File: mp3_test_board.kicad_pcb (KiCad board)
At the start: 2 copper layers, 12 parts, among them U1 RT6222D, U10 OPA1652, U11 LM4562, U12 W25Q128JVSIQ, U13 F1C200S, U2 RT9829, U3 RT4812, U4 RT9525, U5 SN74LVC2G74, U6 RT5750A, U7 RT5750A, U9 WM8741

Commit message: added crystal,backlight regulator and usb nets
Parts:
- removed U1: RT6222D, Package_TO_SOT_SMD:TSOT-23-6
- removed U10: OPA1652, rlib_ic:SOIC-8_3.9x4.9mm_P1.27mm
- removed U11: LM4562, rlib_ic:SOIC-8_3.9x4.9mm_P1.27mm
- removed U12: W25Q128JVSIQ, rlib_ic:SOIC-8_5.23x5.23mm_P1.27mm
- removed U13: F1C200S, rlib_ic:QFN-88_EP_10x10_Pitch0.4mm
- removed U2: RT9829, Package_DFN_QFN:DFN-8_2x2mm_P0.5mm
- removed U3: RT4812, Package_TO_SOT_SMD:TSOT-23-8
- removed U4: RT9525, Package_DFN_QFN:QFN-16-1EP_3x3mm_P0.5mm_EP1.45x1.45mm
- removed U5: SN74LVC2G74, Package_SO:SSOP-8_3.9x5.05mm_P1.27mm
- removed U6, U7: RT5750A, Package_TO_SOT_SMD:SOT-23-5
- removed U9: WM8741, rlib_ic:SSOP-28_5.3x10.2mm_P0.65mm
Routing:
- net Net-(C41-Pad1): track 23.6 -> 0.00 mm
- net +5VA: track 18.8 -> 0.00 mm

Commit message: changed volume buttons
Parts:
- added J2: PJ-3270, rlib_connectors:PJ-3270, F.Cu at (191.1, 128.3)
- added J3: TF01-A, rlib_connectors:TF-01A, F.Cu at (150.3, 130.8)
- added P1: HRO-TYPE-C-31-M-12, rlib_connectors:HRO-TYPE-C-31-M-12, F.Cu at (191.2, 112.5)
- added SW1: TS-1010-C-A, rlib_buttons:TS-1010-X-X, F.Cu at (110.6, 134.0)
- added SW7: TS-1010-C-A, rlib_buttons:TS-1010-X-X, F.Cu at (132.9, 133.9)
- added SW8: TS-1010-C-A, rlib_buttons:TS-1010-X-X, F.Cu at (122.6, 134.0)
- added U1: RT5750A, rlib_power:SOT-23-5, F.Cu at (174.6, 101.0)
- added U10: OPA1652, rlib_ic:SOIC-8_3.9x4.9mm_P1.27mm, F.Cu at (148.0, 92.1)
- added U11: LM4562, rlib_ic:SOIC-8_3.9x4.9mm_P1.27mm, F.Cu at (148.6, 101.6)
- added U12: W25Q128JVSIQ, rlib_ic:SOIC-8_5.23x5.23mm_P1.27mm, F.Cu at (131.4, 116.2)
- added U2: RT9467, rlib_power:WQFN-24-1EP_4x4mm_P0.5mm_EP2.45x2.45mm, F.Cu at (161.3, 120.7)
- added U3: RT4812, rlib_power:TSOT-23-8, F.Cu at (175.3, 116.2)
- added U4: F1C200S, rlib_ic:QFN-88_EP_10x10_Pitch0.4mm, F.Cu at (117.4, 116.1)
- added U5: RT6150, rlib_power:RT6150AGQW, F.Cu at (168.9, 108.6)
- added U6: RT5750A, rlib_power:SOT-23-5, F.Cu at (165.7, 101.0)
- added U7: RT5750A, rlib_power:SOT-23-5, F.Cu at (174.6, 108.0)
- added U8: USBLC6-2SC6, Package_TO_SOT_SMD:SOT-23-6, F.Cu at (136.5, 99.2)
- added U9: WM8741, rlib_ic:SSOP-28_5.3x10.2mm_P0.65mm, F.Cu at (123.2, 102.2)
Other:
- board outline added: 131.4 x 66.7 mm

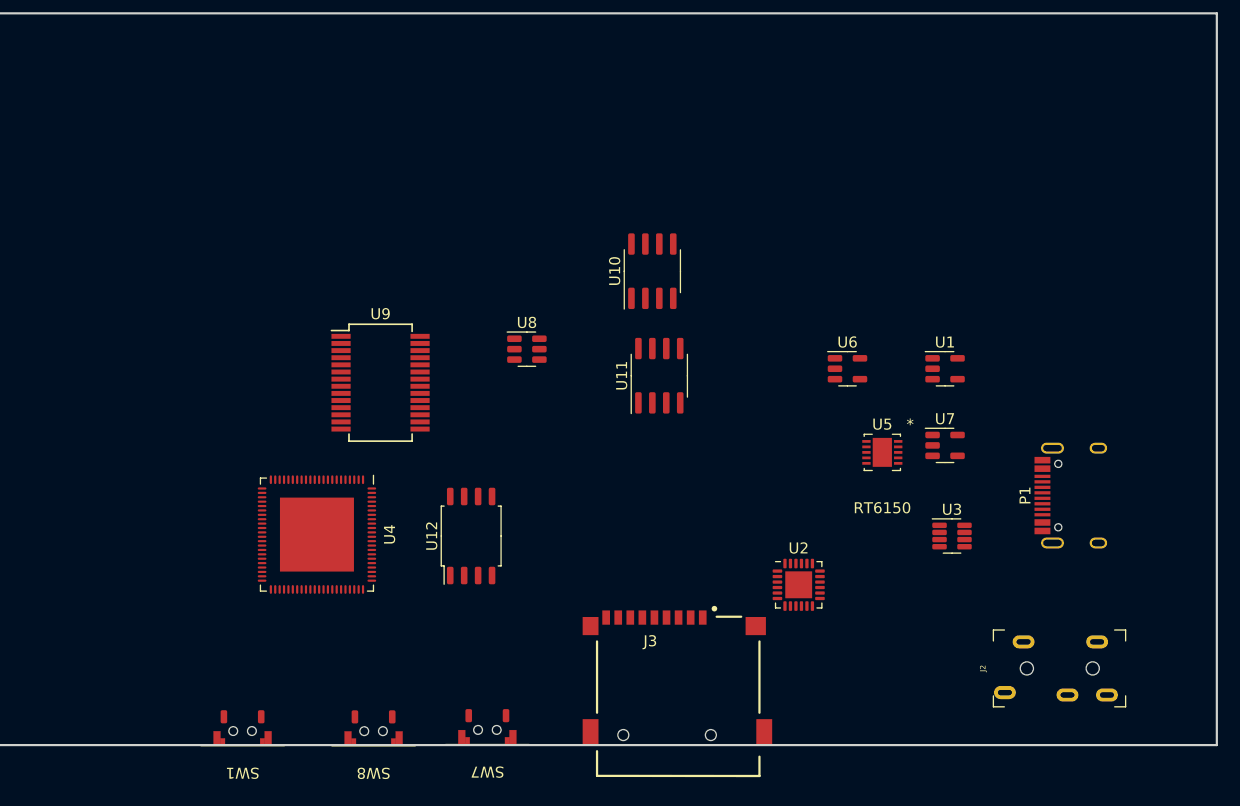
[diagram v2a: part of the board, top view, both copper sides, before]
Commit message: added buttons
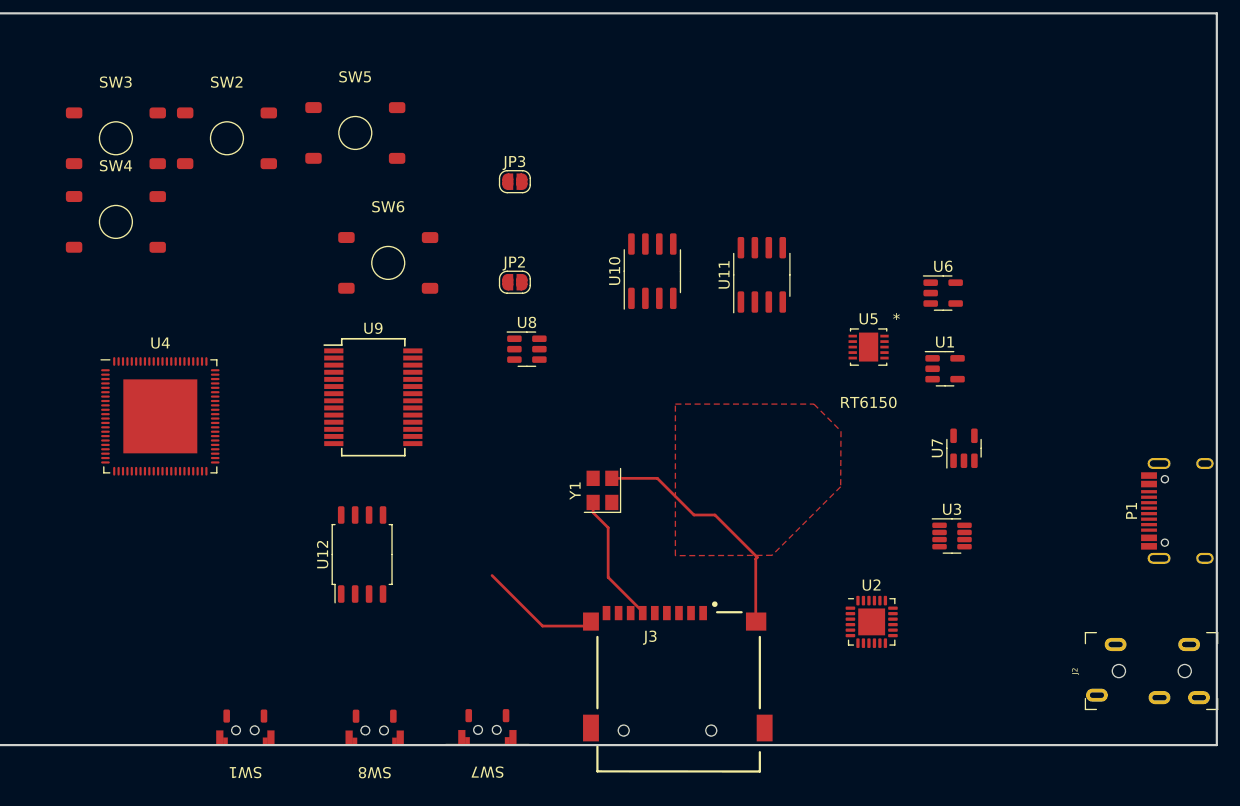
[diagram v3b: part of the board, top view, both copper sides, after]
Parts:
- added JP2: Reset, Jumper:SolderJumper-2_P1.3mm_Open_RoundedPad1.0x1.5mm, F.Cu at (135.4, 93.1)
- added JP3: Jumper_2_Open, Jumper:SolderJumper-2_P1.3mm_Open_RoundedPad1.0x1.5mm, F.Cu at (135.4, 83.9)
- added SW2: TS-1157-X-A, rlib_buttons:TS-1157-X-A, F.Cu at (109.2, 80.0)
- added SW3: TS-1157-X-A, rlib_buttons:TS-1157-X-A, F.Cu at (99.1, 80.0)
- added SW4: TS-1157-X-A, rlib_buttons:TS-1157-X-A, F.Cu at (99.1, 87.6)
- added SW5: TS-1157-X-A, rlib_buttons:TS-1157-X-A, F.Cu at (120.9, 79.5)
- added SW6: TS-1157-X-A, rlib_buttons:TS-1157-X-A, F.Cu at (123.9, 91.3)
- added Y1: Crystal_GND24, rlib_crystals:Crystal_SMD_Abracon_ABM8G-4Pin_3.2x2.5mm, F.Cu at (143.4, 112.0)
- moved U4 17.9 mm to (103.1, 105.3), turned to 0 degrees
- moved U11 13.1 mm to (157.9, 92.4)
- moved U6 11.1 mm to (174.5, 94.1)
- moved U12 10.1 mm to (121.5, 117.9)
- moved P1 9.81 mm to (200.9, 113.9)
- moved U5 9.68 mm to (167.7, 99.0)
- moved J2 8.39 mm to (199.5, 128.5)
- moved U2 7.46 mm to (167.9, 124.0)
- moved U7 1.74 mm to (176.3, 108.2), turned to 90 degrees
- moved U9 1.48 mm to (122.5, 103.6)
- moved J3 0.41 mm to (150.3, 130.4)
- moved SW1 0.26 mm to (110.9, 133.9)
- moved SW8 0.12 mm to (122.7, 133.9)
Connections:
- U4 pad 60: AUDIO_PLUG -> Net-(U4-Pad60)
- U4 pad 62: unconnected-(U4-Pad62) -> AUDIO_PLUG
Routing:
- net GND: track 0.00 -> 45.8 mm
- added copper zone on F.Cu, net /SOC/LCD_D10

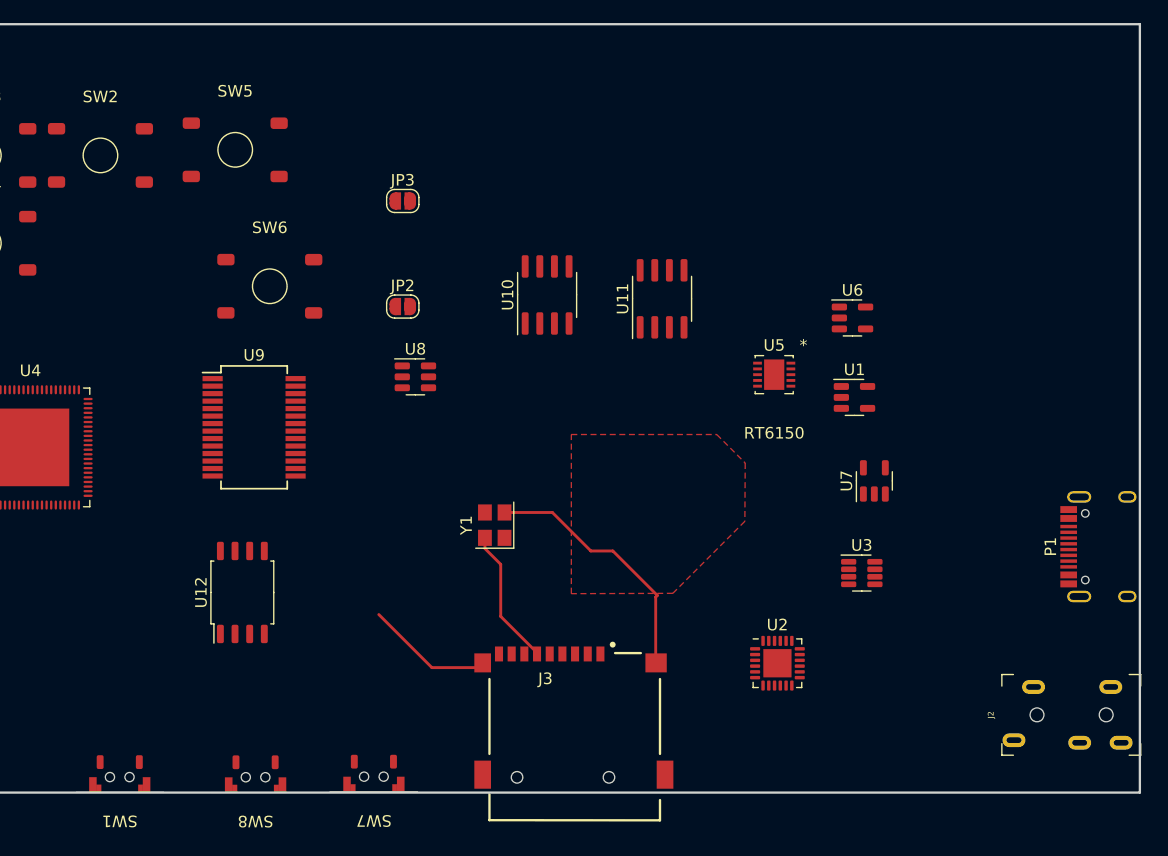
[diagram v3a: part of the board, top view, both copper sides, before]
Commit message: adde power source 3v0, molex connector, restistor footprints
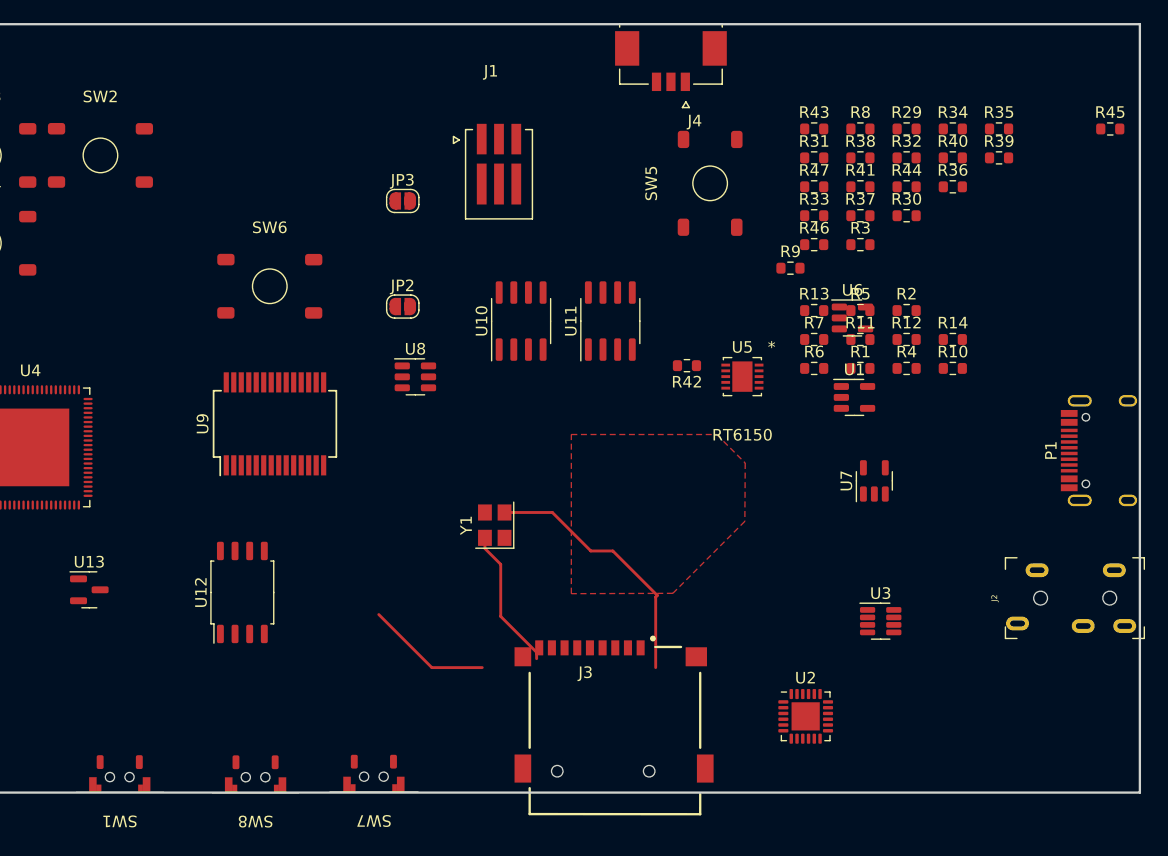
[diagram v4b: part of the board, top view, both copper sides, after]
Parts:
- added J1: 874380343, rlib_connectors:MOLEX_874380343, F.Cu at (143.8, 81.6)
- added J4: 532610371, rlib_connectors:MOLEX_532610371, F.Cu at (158.7, 71.2)
- added R1: R, rlib_passive:R_0603_1608Metric, F.Cu at (175.1, 98.5)
- added R10: R, rlib_passive:R_0603_1608Metric, F.Cu at (183.2, 98.5)
- added R11: R, rlib_passive:R_0603_1608Metric, F.Cu at (175.1, 95.9)
- added R12: R, rlib_passive:R_0603_1608Metric, F.Cu at (179.2, 95.9)
- added R13: R, rlib_passive:R_0603_1608Metric, F.Cu at (171.1, 93.4)
- added R14: R, rlib_passive:R_0603_1608Metric, F.Cu at (183.2, 95.9)
- added R2: R, rlib_passive:R_0603_1608Metric, F.Cu at (179.2, 93.4)
- added R29: R, rlib_passive:R_0603_1608Metric, F.Cu at (179.2, 77.7)
- added R3: R, rlib_passive:R_0603_1608Metric, F.Cu at (175.1, 87.7)
- added R30: R, rlib_passive:R_0603_1608Metric, F.Cu at (179.2, 85.2)
- added R31: R, rlib_passive:R_0603_1608Metric, F.Cu at (171.1, 80.2)
- added R32: R, rlib_passive:R_0603_1608Metric, F.Cu at (179.2, 80.2)
- added R33: R, rlib_passive:R_0603_1608Metric, F.Cu at (171.1, 85.2)
- added R34: R, rlib_passive:R_0603_1608Metric, F.Cu at (183.2, 77.7)
- added R35: R, rlib_passive:R_0603_1608Metric, F.Cu at (187.2, 77.7)
- added R36: R, rlib_passive:R_0603_1608Metric, F.Cu at (183.2, 82.7)
- added R37: R, rlib_passive:R_0603_1608Metric, F.Cu at (175.1, 85.2)
- added R38: R, rlib_passive:R_0603_1608Metric, F.Cu at (175.1, 80.2)
- added R39: R, rlib_passive:R_0603_1608Metric, F.Cu at (187.2, 80.2)
- added R4: R, rlib_passive:R_0603_1608Metric, F.Cu at (179.2, 98.5)
- added R40: R, rlib_passive:R_0603_1608Metric, F.Cu at (183.2, 80.2)
- added R41: R, rlib_passive:R_0603_1608Metric, F.Cu at (175.1, 82.7)
- added R42: R, rlib_passive:R_0603_1608Metric, F.Cu at (160.1, 98.2)
- added R43: R, rlib_passive:R_0603_1608Metric, F.Cu at (171.1, 77.7)
- added R44: R, rlib_passive:R_0603_1608Metric, F.Cu at (179.2, 82.7)
- added R45: R, rlib_passive:R_0603_1608Metric, F.Cu at (196.8, 77.7)
- added R46: R, rlib_passive:R_0603_1608Metric, F.Cu at (171.1, 87.7)
- added R47: R, rlib_passive:R_0603_1608Metric, F.Cu at (171.1, 82.7)
- added R5: R, rlib_passive:R_0603_1608Metric, F.Cu at (175.1, 93.4)
- added R6: R, rlib_passive:R_0603_1608Metric, F.Cu at (171.1, 98.5)
- added R7: R, rlib_passive:R_0603_1608Metric, F.Cu at (171.1, 95.9)
- added R8: R, rlib_passive:R_0603_1608Metric, F.Cu at (175.1, 77.7)
- added R9: R, rlib_passive:R_0603_1608Metric, F.Cu at (169.1, 89.8)
- added U13: XC6206P302MR, rlib_power:SOT-23, F.Cu at (108.2, 117.7)
- moved SW5 41.3 mm to (162.1, 82.4), turned to 90 degrees
- moved J2 10.1 mm to (199.8, 118.4)
- moved P1 8.34 mm to (201.0, 105.6)
- moved U2 5.22 mm to (170.4, 128.6)
- moved U11 4.89 mm to (153.4, 94.3)
- moved U3 4.49 mm to (176.9, 120.4)
- moved J3 3.53 mm to (153.8, 129.9)
- moved U10 3.20 mm to (145.7, 94.3)
- moved U5 2.77 mm to (164.9, 99.2)
- moved U9 1.83 mm to (124.3, 103.3), turned to 90 degrees

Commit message: added winstar display
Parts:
- added C1: C, rlib_passive:C_0603_1608Metric, F.Cu at (209.5, 121.0)
- added C10: C, rlib_passive:C_0603_1608Metric, F.Cu at (209.5, 123.5)
- added C11: C, rlib_passive:C_0603_1608Metric, F.Cu at (193.4, 118.5)
- added C12: C, rlib_passive:C_0603_1608Metric, F.Cu at (197.4, 121.0)
- added C13: C, rlib_passive:C_0603_1608Metric, F.Cu at (201.4, 118.5)
- added C14: C, rlib_passive:C_0603_1608Metric, F.Cu at (201.4, 126.0)
- added C15: 100n, rlib_passive:C_0603_1608Metric, F.Cu at (221.4, 93.5)
- added C16: C, rlib_passive:C_0603_1608Metric, F.Cu at (209.5, 118.5)
- added C17: C, rlib_passive:C_0603_1608Metric, F.Cu at (205.4, 118.5)
- added C18: C, rlib_passive:C_0603_1608Metric, F.Cu at (213.5, 118.5)
- added C19: C, rlib_passive:C_0603_1608Metric, F.Cu at (197.4, 126.0)
- added C2: C, rlib_passive:C_0603_1608Metric, F.Cu at (205.4, 126.0)
- added C20: C, rlib_passive:C_0603_1608Metric, F.Cu at (205.4, 121.0)
- added C21: C, rlib_passive:C_0603_1608Metric, F.Cu at (205.4, 123.5)
- added C22: C, rlib_passive:C_0603_1608Metric, F.Cu at (205.4, 116.0)
- added C26: 0.1u, rlib_passive:C_0603_1608Metric, F.Cu at (226.5, 100.0)
- added C28: 0.1u, rlib_passive:C_0603_1608Metric, F.Cu at (234.5, 97.5)
- added C3: C, rlib_passive:C_0603_1608Metric, F.Cu at (197.4, 116.0)
- added C30: 0.1u, rlib_passive:C_0603_1608Metric, F.Cu at (226.5, 97.5)
- added C32: 0.1u, rlib_passive:C_0603_1608Metric, F.Cu at (234.5, 100.0)
- added C33: 3.3n, rlib_passive:C_0603_1608Metric, F.Cu at (234.5, 95.0)
- added C34: 3.3n, rlib_passive:C_0603_1608Metric, F.Cu at (226.5, 95.0)
- added C37: 0.1u, rlib_passive:C_0603_1608Metric, F.Cu at (230.5, 95.0)
- added C38: 0.1u, rlib_passive:C_0603_1608Metric, F.Cu at (230.5, 100.0)
- added C4: C, rlib_passive:C_0603_1608Metric, F.Cu at (201.4, 123.5)
- added C45: 0.1u, rlib_passive:C_0603_1608Metric, F.Cu at (230.5, 97.5)
- added C46: 0.1u, rlib_passive:C_0603_1608Metric, F.Cu at (152.0, 171.7)
- added C47: 100n, rlib_passive:C_0603_1608Metric, F.Cu at (213.4, 96.0)
- added C48: 100n, rlib_passive:C_0603_1608Metric, F.Cu at (134.4, 175.9)
- added C49: 100n, rlib_passive:C_0603_1608Metric, F.Cu at (205.4, 101.1)
- added C5: C, rlib_passive:C_0603_1608Metric, F.Cu at (193.4, 126.0)
- added C50: 100n, rlib_passive:C_0603_1608Metric, F.Cu at (205.4, 98.5)
- added C51: C, rlib_passive:C_0603_1608Metric, F.Cu at (197.4, 123.5)
- added C52: C, rlib_passive:C_0603_1608Metric, F.Cu at (193.4, 116.0)
- added C53: C, rlib_passive:C_0603_1608Metric, F.Cu at (197.4, 118.5)
- added C54: 100n, rlib_passive:C_0603_1608Metric, F.Cu at (213.4, 93.5)
- added C55: 100n, rlib_passive:C_0603_1608Metric, F.Cu at (142.4, 175.9)
- added C56: 100n, rlib_passive:C_0603_1608Metric, F.Cu at (205.4, 93.5)
- added C57: 100n, rlib_passive:C_0603_1608Metric, F.Cu at (138.4, 175.9)
- added C58: 100n, rlib_passive:C_0603_1608Metric, F.Cu at (209.4, 96.0)
- added C59: 100n, rlib_passive:C_0603_1608Metric, F.Cu at (207.3, 106.1)
- added C6: C, rlib_passive:C_0603_1608Metric, F.Cu at (193.4, 123.5)
- added C60: 100n, rlib_passive:C_0603_1608Metric, F.Cu at (213.4, 98.5)
- added C61: 100n, rlib_passive:C_0603_1608Metric, F.Cu at (195.3, 106.3)
- added C62: 100n, rlib_passive:C_0603_1608Metric, F.Cu at (209.4, 98.5)
- added C63: 100n, rlib_passive:C_0603_1608Metric, F.Cu at (209.4, 101.1)
- added C64: 100n, rlib_passive:C_0603_1608Metric, F.Cu at (130.4, 175.9)
- added C65: 100n, rlib_passive:C_0603_1608Metric, F.Cu at (209.4, 103.6)
- added C66: 100n, rlib_passive:C_0603_1608Metric, F.Cu at (203.3, 106.3)
- added C67: 100n, rlib_passive:C_0603_1608Metric, F.Cu at (199.3, 106.3)
- added C68: 100n, rlib_passive:C_0603_1608Metric, F.Cu at (205.4, 103.6)
- added C69: 100n, rlib_passive:C_0603_1608Metric, F.Cu at (217.4, 93.5)
- added C7: C, rlib_passive:C_0603_1608Metric, F.Cu at (201.4, 116.0)
- added C70: 100n, rlib_passive:C_0603_1608Metric, F.Cu at (217.4, 96.0)
- added C71: 100n, rlib_passive:C_0603_1608Metric, F.Cu at (126.3, 175.9)
- added C74: 100n, rlib_passive:C_0603_1608Metric, F.Cu at (209.4, 93.5)
- added C75: 100n, rlib_passive:C_0603_1608Metric, F.Cu at (205.4, 96.0)
- added C76: C, rlib_passive:C_0603_1608Metric, F.Cu at (201.4, 121.0)
- added C77: C, rlib_passive:C_0603_1608Metric, F.Cu at (193.4, 121.0)
- added C8: C, rlib_passive:C_0603_1608Metric, F.Cu at (209.5, 116.0)
- added C9: C, rlib_passive:C_0603_1608Metric, F.Cu at (213.5, 116.0)
- added REF**: WF24LTYAJDNN0, rlib_lcd:WF24LTYAJDNN0, F.Cu at (108.0, 105.8)
- added REF**: MountingHole_3mm_Pad_Via, MountingHole:MountingHole_3mm_Pad_Via, F.Cu at (148.0, 62.0)
- added REF**: MountingHole_3mm_Pad_Via, MountingHole:MountingHole_3mm_Pad_Via, F.Cu at (149.0, 107.0)
- added REF**: MountingHole_3mm_Pad_Via, MountingHole:MountingHole_3mm_Pad_Via, F.Cu at (44.0, 106.0)
- added REF**: MountingHole_3mm_Pad_Via, MountingHole:MountingHole_3mm_Pad_Via, F.Cu at (45.0, 62.0)
- J2, J3, J4, U10, U11, U12, U13, U2, U4, U5, U9: moved to B.Cu
- moved U2 135.5 mm to (46.0, 75.0), turned to 180 degrees
- moved R3 122.3 mm to (297.0, 98.7)
- moved R37 122.3 mm to (297.0, 96.2)
- moved R41 122.3 mm to (297.0, 93.7)
- moved R8 122.3 mm to (297.0, 88.7)
- moved R29 122.3 mm to (301.0, 88.7)
- moved R30 122.3 mm to (301.0, 96.2)
- moved R34 122.3 mm to (305.0, 88.7)
- moved R35 122.3 mm to (309.0, 88.7)
- moved R36 122.3 mm to (305.0, 93.7)
- moved R38 122.3 mm to (297.0, 91.2)
- moved R42 122.3 mm to (281.9, 109.2)
- moved R44 122.3 mm to (301.0, 93.7)
- moved Y1 122.3 mm to (265.2, 123.1)
- moved JP2 122.3 mm to (257.3, 104.1)
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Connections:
- J4 pad 1: +BATT -> Net-(F1-Pad2)
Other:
- board size 131.4 x 66.7 mm -> 113.1 x 53 mm

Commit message: buttons are changed
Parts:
- P1: moved to B.Cu
- SW2: renamed from SW3; value TS-1157-X-A -> TS-1157-X-F; footprint rlib_buttons:TS-1157-X-A -> rlib_buttons:TS-1157-X-F
- SW3: renamed from SW6; value TS-1157-X-A -> TS-1157-X-F; footprint rlib_buttons:TS-1157-X-A -> rlib_buttons:TS-1157-X-F
- SW4, SW5: value TS-1157-X-A -> TS-1157-X-F; footprint rlib_buttons:TS-1157-X-A -> rlib_buttons:TS-1157-X-F
- SW6: renamed from SW2; value TS-1157-X-A -> TS-1157-X-F; footprint rlib_buttons:TS-1157-X-A -> rlib_buttons:TS-1157-X-F
- moved J4 121.6 mm to (57.0, 98.0), turned to -90 degrees
- moved U12 8.54 mm to (72.0, 91.0)
- moved U4 5.59 mm to (84.0, 91.0)
- moved P1 2.00 mm to (154.1, 95.0), turned to -90 degrees
